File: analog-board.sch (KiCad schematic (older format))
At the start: 491 parts, among them J1 AC IN, J2 OUT, J3 CONN_20X2, P2 CONN_01X02, Q1 2N3906, Q10 2N3906, Q11 2N3906, Q12 2N3906, Q13 2N3906, Q14 2N3906, Q15 2N3906, Q16 2N3906, Q17 NPN, Q18 NPN, Q19 J111, Q2 2N3906, Q20 2N3906, Q3 2N3906, Q4 2N3906, Q5 2N3906, Q6 BCM857BS, Q7 2N3906, Q8 2N3906, Q9 2N3906, U1 LM13700, U10 ADR01, U11 DG212B, U12 DG212B, U13 DG408, U14 DG408, U15 TL072-, U16 DG408, U17 DG408, U18 LM13700, U19 LM13700, U2 LM13700, U20 74HC75, U21 TL072-, U22 TL074-, U23 TL074-, U24 TL074-, U25 TL074-, U26 TL072-, U27 TL074-, U28 TL074-, U29 LM13700, U3 LM13700, U30 LM13700, U31 TL074-, U32 LM13700, U33 TL074-, U34 TL074-, U35 TL074-, U36 74LV573, U38 0 - 10V, U39 TL074-, U4 DG212B, U40 DG419, U41 0 - 10V, U42 10 - 0V, U43 LM7812, U44 LM7912, U45 DG408, U46 7805, U5 TL074-, U6 AD5556, U7 TL072-, U8 TL074-, U9 AD8672

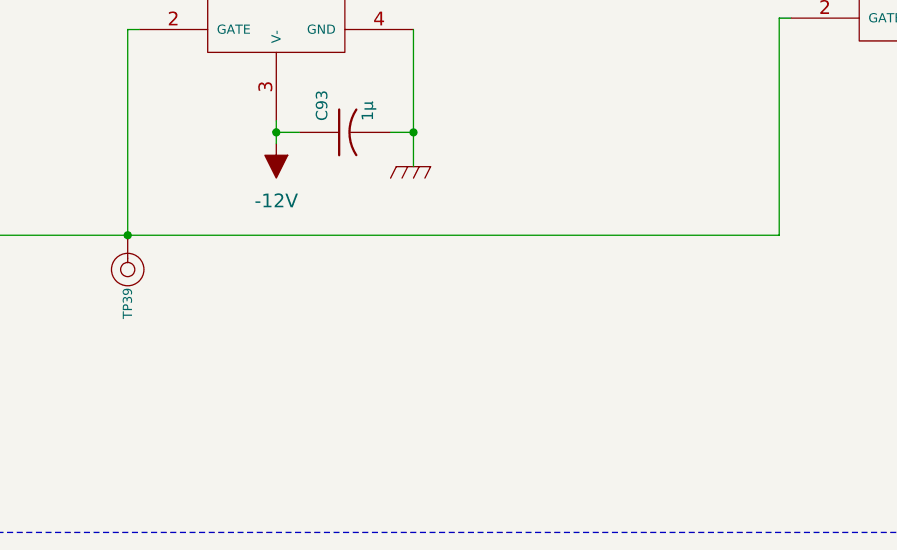
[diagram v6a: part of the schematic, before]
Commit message: changed C47, C48 and C107 packages to 5mm box/0805 combos
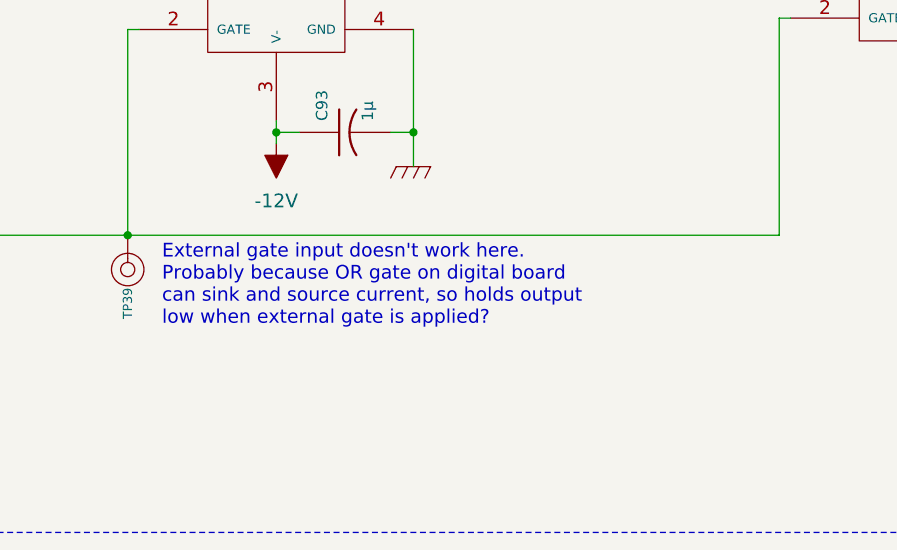
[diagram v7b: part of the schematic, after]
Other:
- note added: "External gate input doesn't work here.\nProbably because OR gate on digital board\ncan sink and source current, so holds output \nlow when external gate is applied?"
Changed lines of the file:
@@
 Text Notes 16450 11100 0    60   ~ 0
 *NOTE: C47 and C48 values: need\nto experiment more with C47 and \nC48 values. Change to dual\nfootprint 0805 and TH.
+Text Notes 31500 31750 0    60   ~ 0
+External gate input doesn't work here.\nProbably because OR gate on digital board\ncan sink and source current, so holds output \nlow when external gate is applied?
 $EndSCHEMATC

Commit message: added resistor dividers for pulse output on VCOs and LFO to get 10Vpp pulse level
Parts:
- added R210: 3.3K, symbol R_US
- added R211, R213: 10K, symbol R_US
- added R212, R214: 9.1K, symbol R_US
- gave numbers to parts that had none: 2
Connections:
- net GND: now also R212.1, R214.1
- net LFO TUNE: now also R210.2; no longer U45.7 (S3)
- net at VCO1.9: now also R213.2; no longer U11.3
- net at VCO2.9: now also R211.2; no longer U12.6
- new net: R213.1, R214.2, U11.3
- new net: R211.1, R212.2, U12.6
- new net: R210.1, U45.7 (S3)
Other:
- note added: "PULSE output divider\nnetwork to get 10 Vpp"
- note added: "PULSE output\ndivider network\nto get 10 Vpp"
- note added: "R210 is to adjust level of pulse out of LFO."
